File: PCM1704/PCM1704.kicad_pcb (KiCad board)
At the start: 4 copper layers, 90 x 90 mm, 143 parts, among them IC1 LT3042, IC2 LT3042, J1 AUDIO OUT, J2 POWER, J3 PROG, J5 I2S IN, U1 PCM1704, U10 LM337, U11 74LVC1G17, U12 LM317, U13 74LVC125APW, U14 TPS7A2033, U2 PCM1704, U3 DF1704, U4 OPA1611, U5 OPA1611, U6 LT3094, U7 ATtiny1614, U8 OPA1612, U9 OPA1612

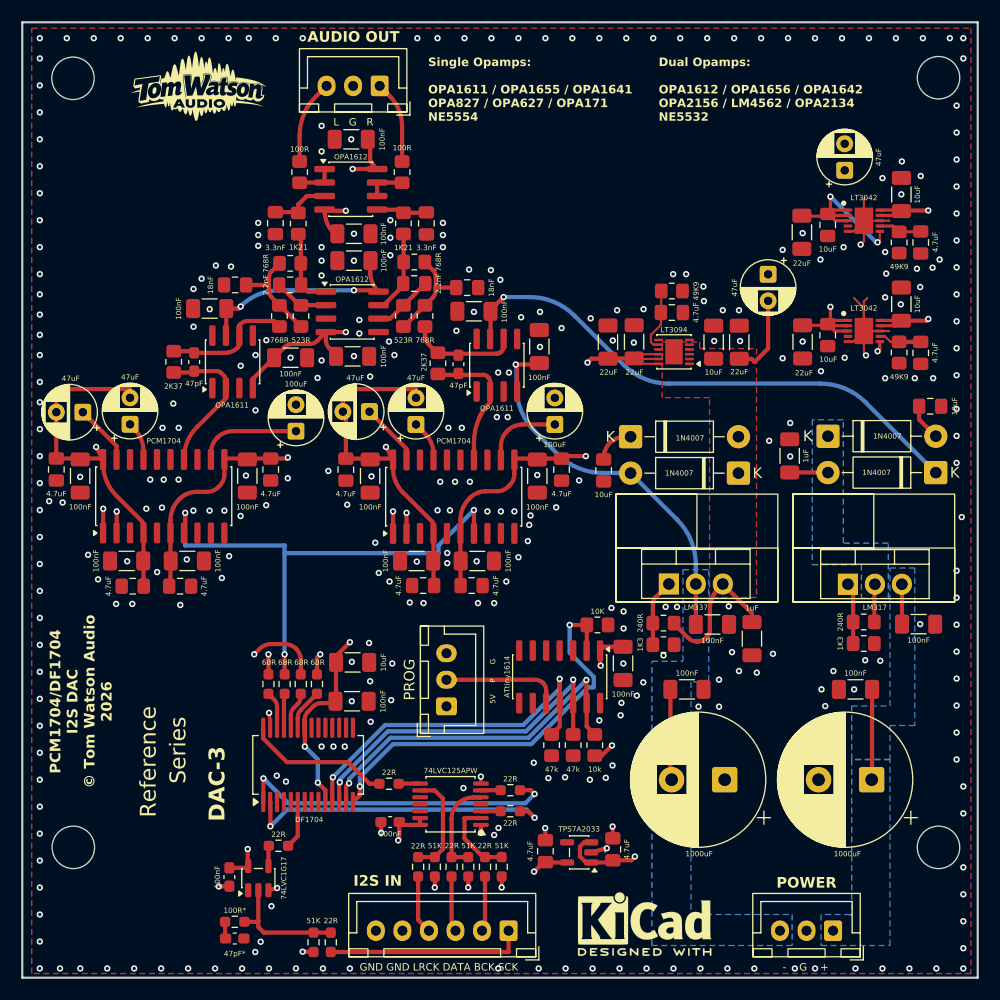
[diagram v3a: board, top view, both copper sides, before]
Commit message: PCM1704: H1 - GND pour on In2/B.Cu, BCLK/DATA re-spaced
Add stitched GND zone on In2 and B.Cu so DF1704->PCM1704 clock/data
tracks have adjacent reference copper (86-96% coverage). Re-route U2
DATA and the U1 branch of BCLK on In2 for >=1.17 mm centre spacing.
DRC (zones refilled) shows only pre-existing items.

Co-Authored-By: Claude Opus 5.5 <noreply@anthropic.com>
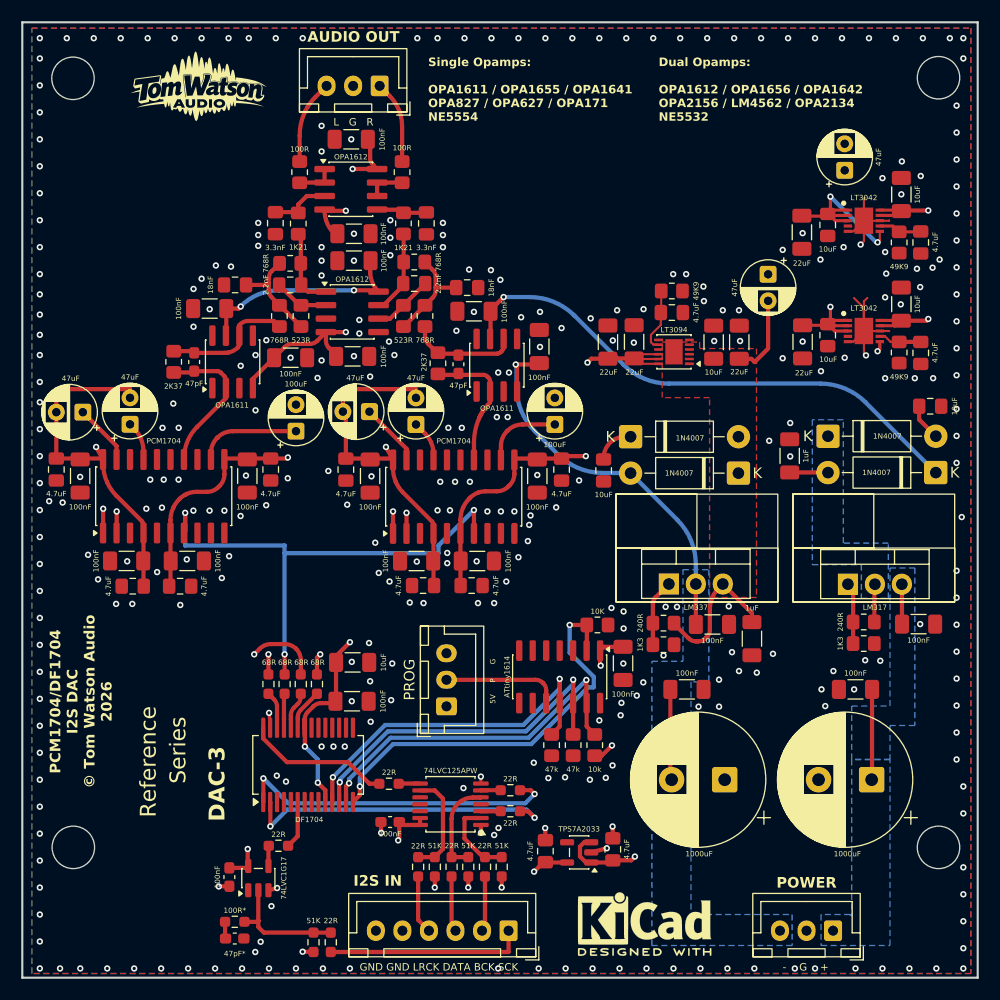
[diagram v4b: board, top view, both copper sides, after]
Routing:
- net Net-(U2-DATA): track 29.4 -> 31.0 mm
- net Net-(U1-BCLK): track 46.6 -> 47.4 mm
- added copper zone on B.Cu, net GND
- added copper zone on In2.Cu, net GND
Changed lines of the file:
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@@
 	)
 	(segment
-		(start 138.211 109.00325)
-		(end 138.211 106.431472)
+		(start 133.9303 113.284)
+		(end 137.2 110.0143)
 		(width 0.4)
 		(layer "In2.Cu")
@@
 	)
 	(segment
-		(start 138.211 106.431472)
-		(end 144.969 99.673472)
+		(start 145.9 98.9)
+		(end 146.939 99.949)
 		(width 0.4)
 		(layer "In2.Cu")
@@
 	)
 	(segment
-		(start 144.969 99.673472)
-		(end 144.969 99.53205)
+		(start 137.2 106.2)
+		(end 144.5 98.9)
 		(width 0.4)
 		(layer "In2.Cu")
@@
 	)
 	(segment
-		(start 144.969 99.53205)
-		(end 145.37905 99.122)
+		(start 144.5 98.9)
+		(end 145.9 98.9)
 		(width 0.4)
 		(layer "In2.Cu")
@@
 	)
 	(segment
-		(start 133.93025 113.284)
-		(end 138.211 109.00325)
-		(width 0.4)
-		(layer "In2.Cu")
-		(net "Net-(U1-BCLK)")
-	)
-	(segment
-		(start 145.37905 99.122)
-		(end 146.112 99.122)
-		(width 0.4)
-		(layer "In2.Cu")
-		(net "Net-(U1-BCLK)")
-	)
-	(segment
-		(start 146.112 99.122)
-		(end 146.939 99.949)
+		(start 137.2 110.0143)
+		(end 137.2 106.2)
 		(width 0.4)
 		(layer "In2.Cu")
@@
 	)
 	(segment
+		(start 132.588 113.588)
+		(end 121 102)
+		(width 0.4)
+		(layer "In2.Cu")
+		(net "Net-(U2-DATA)")
+	)
+	(segment
+		(start 121 102)
+		(end 118.364 102)
+		(width 0.4)
+		(layer "In2.Cu")
+		(net "Net-(U2-DATA)")
+	)
+	(segment
+		(start 118.364 102)
+		(end 118.364 99.568)
+		(width 0.4)
+		(layer "In2.Cu")
+		(net "Net-(U2-DATA)")
+	)
+	(segment
 		(start 132.588 113.284)
-		(end 132.588 112.790278)
-		(width 0.4)
-		(layer "In2.Cu")
-		(net "Net-(U2-DATA)")
-	)
-	(segment
-		(start 118.39005 99.568)
-		(end 118.364 99.568)
-		(width 0.4)
-		(layer "In2.Cu")
-		(net "Net-(U2-DATA)")
-	)
-	(segment
-		(start 120.319722 100.522)
-		(end 119.34405 100.522)
-		(width 0.4)
-		(layer "In2.Cu")
-		(net "Net-(U2-DATA)")
-	)
-	(segment
-		(start 119.34405 100.522)
-		(end 118.39005 99.568)
-		(width 0.4)
-		(layer "In2.Cu")
-		(net "Net-(U2-DATA)")
-	)
-	(segment
-		(start 132.588 112.790278)
-		(end 120.319722 100.522)
+		(end 132.588 113.588)
 		(width 0.4)
 		(layer "In2.Cu")
@@
 			)
 		)
+	)
+	(zone
+		(net "GND")
+		(layers "B.Cu" "In2.Cu")
+		(name "GND_REF_IN2_BCU")
+		(hatch edge 0.5)
+		(connect_pads
+			(clearance 0.2)
+		)
+		(min_thickness 0.2)
+		(fill yes
+			(thermal_gap 0.2)
+			(thermal_bridge_width 0.2)
+			(island_removal_mode 0)
+		)
+		(polygon
+			(pts
+				(xy 200.1012 54.3052) (xy 200.1012 143.351962) (xy 111.633 143.351962) (xy 111.633 54.3052)
+			)
+		)
